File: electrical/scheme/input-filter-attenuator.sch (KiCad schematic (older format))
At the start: 13 parts, among them U4 AD8672

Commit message: a
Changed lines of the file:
@@
 $Descr A4 11693 8268
 encoding utf-8
-Sheet 2 7
+Sheet 4 7
 Title ""
 Date ""
@@
 AR Path="/55AAFE8D/55A8C542" Ref="U6"  Part="1"
 AR Path="/55AAFE9C/55A8C542" Ref="U7"  Part="1"
-F 0 "U7" H 5600 3650 60  0000 C CNN
+F 0 "U6" H 5600 3650 60  0000 C CNN
 F 1 "AD8672" H 5600 4050 60  0000 C CNN
 F 2 "Housings_SOIC:SOIC-8_3.9x4.9mm_Pitch1.27mm" H 5300 3850 60  0001 C CNN
@@
 AR Path="/55AAFE8D/55A8C549" Ref="U6"  Part="2"
 AR Path="/55AAFE9C/55A8C549" Ref="U7"  Part="2"
-F 0 "U7" H 8700 3850 60  0000 C CNN
+F 0 "U6" H 8700 3850 60  0000 C CNN
 F 1 "AD8672" H 8700 4250 60  0000 C CNN
 F 2 "Housings_SOIC:SOIC-8_3.9x4.9mm_Pitch1.27mm" H 8400 4050 60  0001 C CNN
@@
 AR Path="/55AAFE8D/55A8C74B" Ref="R57"  Part="1"
 AR Path="/55AAFE9C/55A8C74B" Ref="R63"  Part="1"
-F 0 "R63" V 5330 2800 50  0000 C CNN
+F 0 "R57" V 5330 2800 50  0000 C CNN
 F 1 "16 5%" V 5250 2800 50  0000 C CNN
 F 2 "Resistors_SMD:R_0805_HandSoldering" V 5180 2800 30  0001 C CNN
@@
 AR Path="/55AAFE8D/55A8C77D" Ref="C54"  Part="1"
 AR Path="/55AAFE9C/55A8C77D" Ref="C60"  Part="1"
-F 0 "C60" H 5025 3150 50  0000 L CNN
+F 0 "C54" H 5025 3150 50  0000 L CNN
 F 1 "100n" H 5025 2950 50  0000 L CNN
 F 2 "Capacitors_SMD:C_0805_HandSoldering" H 5038 2900 30  0001 C CNN
@@
 AR Path="/55AAFE8D/55A8C85F" Ref="#PWR0143"  Part="1"
 AR Path="/55AAFE9C/55A8C85F" Ref="#PWR0149"  Part="1"
-F 0 "#PWR0149" H 4650 2900 50  0001 C CNN
+F 0 "#PWR0143" H 4650 2900 50  0001 C CNN
 F 1 "GNDA" H 4650 3000 50  0000 C CNN
 F 2 "" H 4650 3150 60  0000 C CNN
@@
 AR Path="/55AAFE8D/55A8C8A7" Ref="R58"  Part="1"
 AR Path="/55AAFE9C/55A8C8A7" Ref="R64"  Part="1"
-F 0 "R64" V 5330 4800 50  0000 C CNN
+F 0 "R58" V 5330 4800 50  0000 C CNN
 F 1 "16 5%" V 5250 4800 50  0000 C CNN
 F 2 "Resistors_SMD:R_0805_HandSoldering" V 5180 4800 30  0001 C CNN
@@
 AR Path="/55AAFE8D/55A8CC9D" Ref="C55"  Part="1"
 AR Path="/55AAFE9C/55A8CC9D" Ref="C61"  Part="1"
-F 0 "C61" H 5025 4650 50  0000 L CNN
+F 0 "C55" H 5025 4650 50  0000 L CNN
 F 1 "100n" H 5025 4450 50  0000 L CNN
 F 2 "Capacitors_SMD:C_0805_HandSoldering" H 5038 4400 30  0001 C CNN
@@
 AR Path="/55AAFE8D/55A8CCA5" Ref="#PWR0144"  Part="1"
 AR Path="/55AAFE9C/55A8CCA5" Ref="#PWR0150"  Part="1"
-F 0 "#PWR0150" H 4650 4400 50  0001 C CNN
+F 0 "#PWR0144" H 4650 4400 50  0001 C CNN
 F 1 "GNDA" H 4650 4500 50  0000 C CNN
 F 2 "" H 4650 4650 60  0000 C CNN
@@
 AR Path="/55AAFE8D/55A8D6B2" Ref="R55"  Part="1"
 AR Path="/55AAFE9C/55A8D6B2" Ref="R61"  Part="1"
-F 0 "R61" V 3180 3650 50  0000 C CNN
+F 0 "R55" V 3180 3650 50  0000 C CNN
 F 1 "806 1%" V 3100 3650 50  0000 C CNN
 F 2 "Resistors_SMD:R_0805_HandSoldering" V 3030 3650 30  0001 C CNN
@@
 AR Path="/55AAFE8D/55A8D707" Ref="R56"  Part="1"
 AR Path="/55AAFE9C/55A8D707" Ref="R62"  Part="1"
-F 0 "R62" V 3680 3650 50  0000 C CNN
+F 0 "R56" V 3680 3650 50  0000 C CNN
 F 1 "1k91 1%" V 3600 3650 50  0000 C CNN
 F 2 "Resistors_SMD:R_0805_HandSoldering" V 3530 3650 30  0001 C CNN
@@
 AR Path="/55AAFE8D/55A8D733" Ref="C53"  Part="1"
 AR Path="/55AAFE9C/55A8D733" Ref="C59"  Part="1"
-F 0 "C59" H 3875 4000 50  0000 L CNN
+F 0 "C53" H 3875 4000 50  0000 L CNN
 F 1 "22n" H 3875 3800 50  0000 L CNN
 F 2 "Capacitors_SMD:C_0805_HandSoldering" H 3888 3750 30  0001 C CNN
@@
 AR Path="/55AAFE8D/55A8D76D" Ref="C52"  Part="1"
 AR Path="/55AAFE9C/55A8D76D" Ref="C58"  Part="1"
-F 0 "C58" H 3375 3450 50  0000 L CNN
+F 0 "C52" H 3375 3450 50  0000 L CNN
 F 1 "3u3" H 3375 3250 50  0000 L CNN
 F 2 "Capacitors_SMD:C_0805_HandSoldering" H 3388 3200 30  0001 C CNN
@@
 AR Path="/55AAFE8D/55A8D8D4" Ref="R59"  Part="1"
 AR Path="/55AAFE9C/55A8D8D4" Ref="R65"  Part="1"
-F 0 "R65" V 6280 3850 50  0000 C CNN
+F 0 "R59" V 6280 3850 50  0000 C CNN
 F 1 "9k31 1%" V 6200 3850 50  0000 C CNN
 F 2 "Resistors_SMD:R_0805_HandSoldering" V 6130 3850 30  0001 C CNN
@@
 AR Path="/55AAFE8D/55A8DA7D" Ref="R60"  Part="1"
 AR Path="/55AAFE9C/55A8DA7D" Ref="R66"  Part="1"
-F 0 "R66" V 6780 3850 50  0000 C CNN
+F 0 "R60" V 6780 3850 50  0000 C CNN
 F 1 "21k 1%" V 6700 3850 50  0000 C CNN
 F 2 "Resistors_SMD:R_0805_HandSoldering" V 6630 3850 30  0001 C CNN
@@
 AR Path="/55AAFE8D/55A8DD2D" Ref="C56"  Part="1"
 AR Path="/55AAFE9C/55A8DD2D" Ref="C62"  Part="1"
-F 0 "C62" H 6475 3700 50  0000 L CNN
+F 0 "C56" H 6475 3700 50  0000 L CNN
 F 1 "120n" H 6475 3500 50  0000 L CNN
 F 2 "Capacitors_SMD:C_0805_HandSoldering" H 6488 3450 30  0001 C CNN
@@
 AR Path="/55AAFE8D/55A8DF47" Ref="C57"  Part="1"
 AR Path="/55AAFE9C/55A8DF47" Ref="C63"  Part="1"
-F 0 "C63" H 7075 4300 50  0000 L CNN
+F 0 "C57" H 7075 4300 50  0000 L CNN
 F 1 "22n" H 7075 4100 50  0000 L CNN
 F 2 "Capacitors_SMD:C_0805_HandSoldering" H 7088 4050 30  0001 C CNN
@@
 AR Path="/55AAFE8D/55A8F5C0" Ref="#PWR0145"  Part="1"
 AR Path="/55AAFE9C/55A8F5C0" Ref="#PWR0151"  Part="1"
-F 0 "#PWR0151" H 7050 4300 50  0001 C CNN
+F 0 "#PWR0145" H 7050 4300 50  0001 C CNN
 F 1 "GNDA" H 7050 4400 50  0000 C CNN
 F 2 "" H 7050 4550 60  0000 C CNN
@@
 AR Path="/55AAFE8D/55A8F5EF" Ref="#PWR0146"  Part="1"
 AR Path="/55AAFE9C/55A8F5EF" Ref="#PWR0152"  Part="1"
-F 0 "#PWR0152" H 3850 4000 50  0001 C CNN
+F 0 "#PWR0146" H 3850 4000 50  0001 C CNN
 F 1 "GNDA" H 3850 4100 50  0000 C CNN
 F 2 "" H 3850 4250 60  0000 C CNN
@@
 AR Path="/55AAFE8D/55BB3EFD" Ref="#FLG0147"  Part="1"
 AR Path="/55AAFE9C/55BB3EFD" Ref="#FLG0153"  Part="1"
-F 0 "#FLG0153" H 5600 3045 50  0001 C CNN
+F 0 "#FLG0147" H 5600 3045 50  0001 C CNN
 F 1 "PWR_FLAG" H 5600 3130 50  0000 C CNN
 F 2 "" H 5600 2950 60  0000 C CNN
@@
 AR Path="/55A8BFF5/55BB3F68" Ref="#FLG0136"  Part="1"
 AR Path="/55AAFE9C/55BB3F68" Ref="#FLG0154"  Part="1"
-F 0 "#FLG0154" H 5600 4745 50  0001 C CNN
+F 0 "#FLG0148" H 5600 4745 50  0001 C CNN
 F 1 "PWR_FLAG" H 5600 4830 50  0000 C CNN
 F 2 "" H 5600 4650 60  0000 C CNN

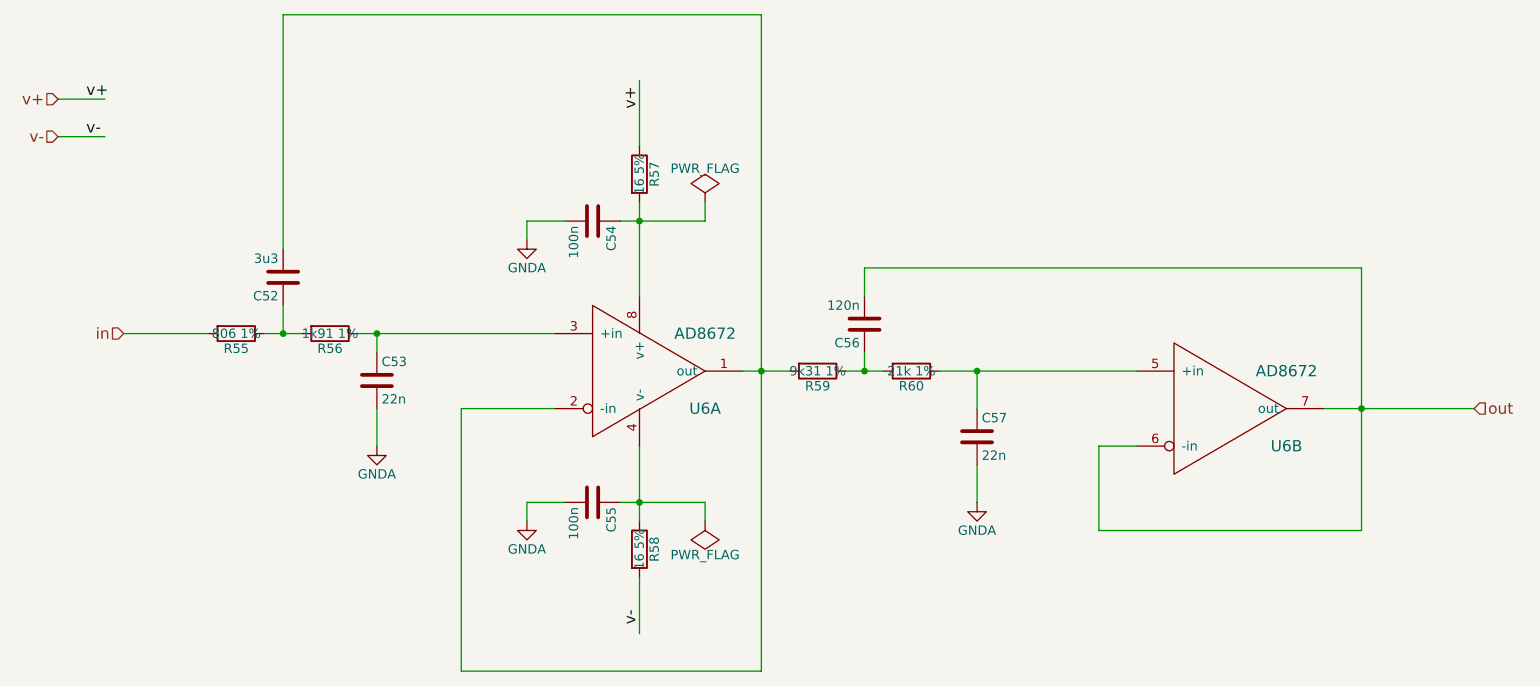
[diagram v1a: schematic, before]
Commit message: Inserted holding screw holes.
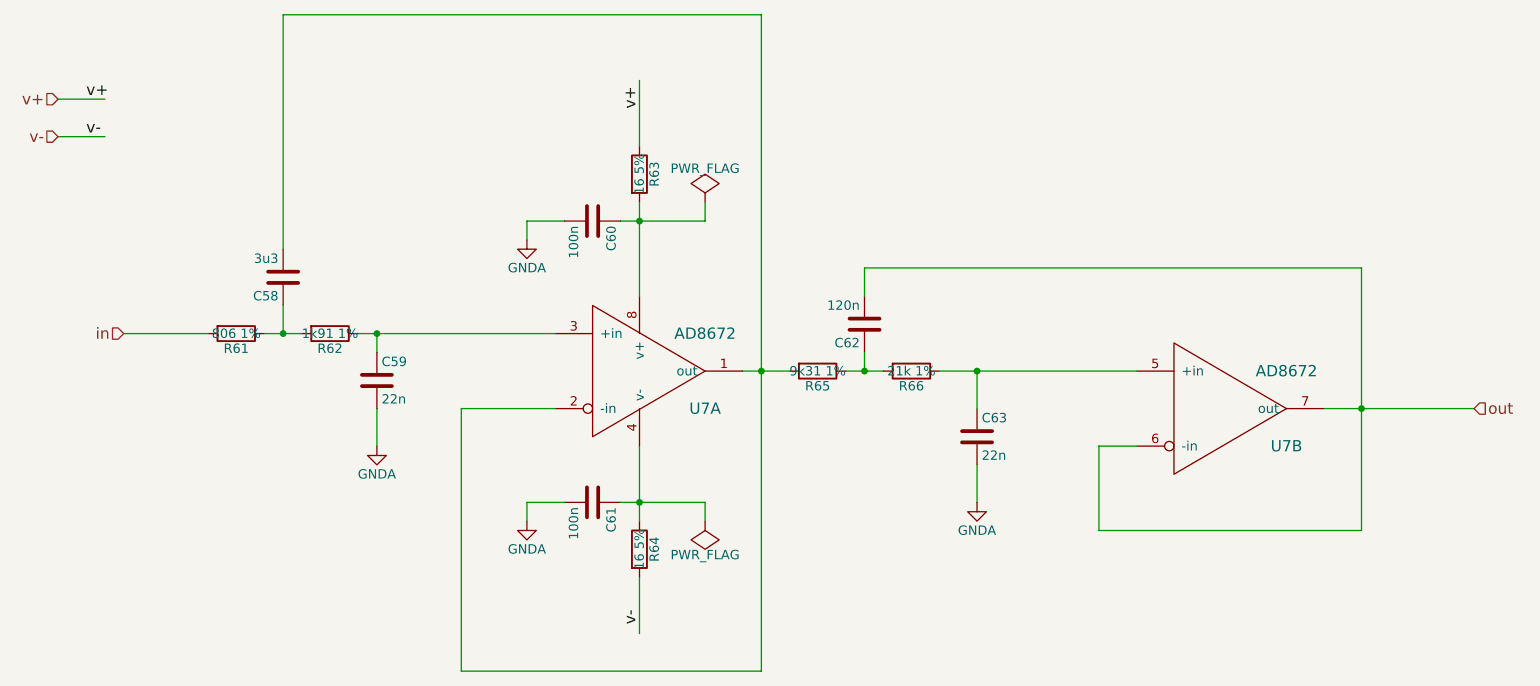
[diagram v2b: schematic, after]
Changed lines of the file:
@@
 $Descr A4 11693 8268
 encoding utf-8
-Sheet 4 7
+Sheet 5 7
 Title ""
 Date ""
@@
 AR Path="/55AAFE8D/55A8C542" Ref="U6"  Part="1"
 AR Path="/55AAFE9C/55A8C542" Ref="U7"  Part="1"
-F 0 "U6" H 5600 3650 60  0000 C CNN
+F 0 "U7" H 5600 3650 60  0000 C CNN
 F 1 "AD8672" H 5600 4050 60  0000 C CNN
 F 2 "Housings_SOIC:SOIC-8_3.9x4.9mm_Pitch1.27mm" H 5300 3850 60  0001 C CNN
@@
 AR Path="/55AAFE8D/55A8C549" Ref="U6"  Part="2"
 AR Path="/55AAFE9C/55A8C549" Ref="U7"  Part="2"
-F 0 "U6" H 8700 3850 60  0000 C CNN
+F 0 "U7" H 8700 3850 60  0000 C CNN
 F 1 "AD8672" H 8700 4250 60  0000 C CNN
 F 2 "Housings_SOIC:SOIC-8_3.9x4.9mm_Pitch1.27mm" H 8400 4050 60  0001 C CNN
@@
 AR Path="/55AAFE8D/55A8C74B" Ref="R57"  Part="1"
 AR Path="/55AAFE9C/55A8C74B" Ref="R63"  Part="1"
-F 0 "R57" V 5330 2800 50  0000 C CNN
+F 0 "R63" V 5330 2800 50  0000 C CNN
 F 1 "16 5%" V 5250 2800 50  0000 C CNN
 F 2 "Resistors_SMD:R_0805_HandSoldering" V 5180 2800 30  0001 C CNN
@@
 AR Path="/55AAFE8D/55A8C77D" Ref="C54"  Part="1"
 AR Path="/55AAFE9C/55A8C77D" Ref="C60"  Part="1"
-F 0 "C54" H 5025 3150 50  0000 L CNN
+F 0 "C60" H 5025 3150 50  0000 L CNN
 F 1 "100n" H 5025 2950 50  0000 L CNN
 F 2 "Capacitors_SMD:C_0805_HandSoldering" H 5038 2900 30  0001 C CNN
@@
 	4650 3050 4650 3150
 $Comp
-L GNDA #PWR0131
+L GNDA #PWR0135
 U 1 1 55A8C85F
 P 4650 3150
-AR Path="/55A8BFF5/55A8C85F" Ref="#PWR0131"  Part="1"
-AR Path="/55AAF91E/55A8C85F" Ref="#PWR0137"  Part="1"
-AR Path="/55AAFE8D/55A8C85F" Ref="#PWR0143"  Part="1"
-AR Path="/55AAFE9C/55A8C85F" Ref="#PWR0149"  Part="1"
-F 0 "#PWR0143" H 4650 2900 50  0001 C CNN
+AR Path="/55A8BFF5/55A8C85F" Ref="#PWR0135"  Part="1"
+AR Path="/55AAF91E/55A8C85F" Ref="#PWR0141"  Part="1"
+AR Path="/55AAFE8D/55A8C85F" Ref="#PWR0147"  Part="1"
+AR Path="/55AAFE9C/55A8C85F" Ref="#PWR0153"  Part="1"
+F 0 "#PWR0153" H 4650 2900 50  0001 C CNN
 F 1 "GNDA" H 4650 3000 50  0000 C CNN
 F 2 "" H 4650 3150 60  0000 C CNN
@@
 AR Path="/55AAFE8D/55A8C8A7" Ref="R58"  Part="1"
 AR Path="/55AAFE9C/55A8C8A7" Ref="R64"  Part="1"
-F 0 "R58" V 5330 4800 50  0000 C CNN
+F 0 "R64" V 5330 4800 50  0000 C CNN
 F 1 "16 5%" V 5250 4800 50  0000 C CNN
 F 2 "Resistors_SMD:R_0805_HandSoldering" V 5180 4800 30  0001 C CNN
@@
 AR Path="/55AAFE8D/55A8CC9D" Ref="C55"  Part="1"
 AR Path="/55AAFE9C/55A8CC9D" Ref="C61"  Part="1"
-F 0 "C55" H 5025 4650 50  0000 L CNN
+F 0 "C61" H 5025 4650 50  0000 L CNN
 F 1 "100n" H 5025 4450 50  0000 L CNN
 F 2 "Capacitors_SMD:C_0805_HandSoldering" H 5038 4400 30  0001 C CNN
@@
 	4650 4550 4650 4650
 $Comp
-L GNDA #PWR0132
+L GNDA #PWR0136
 U 1 1 55A8CCA5
 P 4650 4650
-AR Path="/55A8BFF5/55A8CCA5" Ref="#PWR0132"  Part="1"
-AR Path="/55AAF91E/55A8CCA5" Ref="#PWR0138"  Part="1"
-AR Path="/55AAFE8D/55A8CCA5" Ref="#PWR0144"  Part="1"
-AR Path="/55AAFE9C/55A8CCA5" Ref="#PWR0150"  Part="1"
-F 0 "#PWR0144" H 4650 4400 50  0001 C CNN
+AR Path="/55A8BFF5/55A8CCA5" Ref="#PWR0136"  Part="1"
+AR Path="/55AAF91E/55A8CCA5" Ref="#PWR0142"  Part="1"
+AR Path="/55AAFE8D/55A8CCA5" Ref="#PWR0148"  Part="1"
+AR Path="/55AAFE9C/55A8CCA5" Ref="#PWR0154"  Part="1"
+F 0 "#PWR0154" H 4650 4400 50  0001 C CNN
 F 1 "GNDA" H 4650 4500 50  0000 C CNN
 F 2 "" H 4650 4650 60  0000 C CNN
@@
 AR Path="/55AAFE8D/55A8D6B2" Ref="R55"  Part="1"
 AR Path="/55AAFE9C/55A8D6B2" Ref="R61"  Part="1"
-F 0 "R55" V 3180 3650 50  0000 C CNN
+F 0 "R61" V 3180 3650 50  0000 C CNN
 F 1 "806 1%" V 3100 3650 50  0000 C CNN
 F 2 "Resistors_SMD:R_0805_HandSoldering" V 3030 3650 30  0001 C CNN
@@
 AR Path="/55AAFE8D/55A8D707" Ref="R56"  Part="1"
 AR Path="/55AAFE9C/55A8D707" Ref="R62"  Part="1"
-F 0 "R56" V 3680 3650 50  0000 C CNN
+F 0 "R62" V 3680 3650 50  0000 C CNN
 F 1 "1k91 1%" V 3600 3650 50  0000 C CNN
 F 2 "Resistors_SMD:R_0805_HandSoldering" V 3530 3650 30  0001 C CNN
@@
 AR Path="/55AAFE8D/55A8D733" Ref="C53"  Part="1"
 AR Path="/55AAFE9C/55A8D733" Ref="C59"  Part="1"
-F 0 "C53" H 3875 4000 50  0000 L CNN
+F 0 "C59" H 3875 4000 50  0000 L CNN
 F 1 "22n" H 3875 3800 50  0000 L CNN
 F 2 "Capacitors_SMD:C_0805_HandSoldering" H 3888 3750 30  0001 C CNN
@@
 AR Path="/55AAFE8D/55A8D76D" Ref="C52"  Part="1"
 AR Path="/55AAFE9C/55A8D76D" Ref="C58"  Part="1"
-F 0 "C52" H 3375 3450 50  0000 L CNN
+F 0 "C58" H 3375 3450 50  0000 L CNN
 F 1 "3u3" H 3375 3250 50  0000 L CNN
 F 2 "Capacitors_SMD:C_0805_HandSoldering" H 3388 3200 30  0001 C CNN
@@
 AR Path="/55AAFE8D/55A8D8D4" Ref="R59"  Part="1"
 AR Path="/55AAFE9C/55A8D8D4" Ref="R65"  Part="1"
-F 0 "R59" V 6280 3850 50  0000 C CNN
+F 0 "R65" V 6280 3850 50  0000 C CNN
 F 1 "9k31 1%" V 6200 3850 50  0000 C CNN
 F 2 "Resistors_SMD:R_0805_HandSoldering" V 6130 3850 30  0001 C CNN
@@
 AR Path="/55AAFE8D/55A8DA7D" Ref="R60"  Part="1"
 AR Path="/55AAFE9C/55A8DA7D" Ref="R66"  Part="1"
-F 0 "R60" V 6780 3850 50  0000 C CNN
+F 0 "R66" V 6780 3850 50  0000 C CNN
 F 1 "21k 1%" V 6700 3850 50  0000 C CNN
 F 2 "Resistors_SMD:R_0805_HandSoldering" V 6630 3850 30  0001 C CNN
@@
 AR Path="/55AAFE8D/55A8DD2D" Ref="C56"  Part="1"
 AR Path="/55AAFE9C/55A8DD2D" Ref="C62"  Part="1"
-F 0 "C56" H 6475 3700 50  0000 L CNN
+F 0 "C62" H 6475 3700 50  0000 L CNN
 F 1 "120n" H 6475 3500 50  0000 L CNN
 F 2 "Capacitors_SMD:C_0805_HandSoldering" H 6488 3450 30  0001 C CNN
@@
 AR Path="/55AAFE8D/55A8DF47" Ref="C57"  Part="1"
 AR Path="/55AAFE9C/55A8DF47" Ref="C63"  Part="1"
-F 0 "C57" H 7075 4300 50  0000 L CNN
+F 0 "C63" H 7075 4300 50  0000 L CNN
 F 1 "22n" H 7075 4100 50  0000 L CNN
 F 2 "Capacitors_SMD:C_0805_HandSoldering" H 7088 4050 30  0001 C CNN
@@
 Connection ~ 9100 4050
 $Comp
-L GNDA #PWR0133
+L GNDA #PWR0137
 U 1 1 55A8F5C0
 P 7050 4550
-AR Path="/55A8BFF5/55A8F5C0" Ref="#PWR0133"  Part="1"
-AR Path="/55AAF91E/55A8F5C0" Ref="#PWR0139"  Part="1"
-AR Path="/55AAFE8D/55A8F5C0" Ref="#PWR0145"  Part="1"
-AR Path="/55AAFE9C/55A8F5C0" Ref="#PWR0151"  Part="1"
-F 0 "#PWR0145" H 7050 4300 50  0001 C CNN
+AR Path="/55A8BFF5/55A8F5C0" Ref="#PWR0137"  Part="1"
+AR Path="/55AAF91E/55A8F5C0" Ref="#PWR0143"  Part="1"
+AR Path="/55AAFE8D/55A8F5C0" Ref="#PWR0149"  Part="1"
+AR Path="/55AAFE9C/55A8F5C0" Ref="#PWR0155"  Part="1"
+F 0 "#PWR0155" H 7050 4300 50  0001 C CNN
 F 1 "GNDA" H 7050 4400 50  0000 C CNN
 F 2 "" H 7050 4550 60  0000 C CNN
@@
 $EndComp
 $Comp
-L GNDA #PWR0134
+L GNDA #PWR0138
 U 1 1 55A8F5EF
 P 3850 4250
-AR Path="/55A8BFF5/55A8F5EF" Ref="#PWR0134"  Part="1"
-AR Path="/55AAF91E/55A8F5EF" Ref="#PWR0140"  Part="1"
-AR Path="/55AAFE8D/55A8F5EF" Ref="#PWR0146"  Part="1"
-AR Path="/55AAFE9C/55A8F5EF" Ref="#PWR0152"  Part="1"
-F 0 "#PWR0146" H 3850 4000 50  0001 C CNN
+AR Path="/55A8BFF5/55A8F5EF" Ref="#PWR0138"  Part="1"
+AR Path="/55AAF91E/55A8F5EF" Ref="#PWR0144"  Part="1"
+AR Path="/55AAFE8D/55A8F5EF" Ref="#PWR0150"  Part="1"
+AR Path="/55AAFE9C/55A8F5EF" Ref="#PWR0156"  Part="1"
+F 0 "#PWR0156" H 3850 4000 50  0001 C CNN
 F 1 "GNDA" H 3850 4100 50  0000 C CNN
 F 2 "" H 3850 4250 60  0000 C CNN
@@
 	7700 4250 7900 4250
 $Comp
-L PWR_FLAG #FLG0135
+L PWR_FLAG #FLG0139
 U 1 1 55BB3EFD
 P 5600 2950
-AR Path="/55A8BFF5/55BB3EFD" Ref="#FLG0135"  Part="1"
-AR Path="/55AAF91E/55BB3EFD" Ref="#FLG0141"  Part="1"
-AR Path="/55AAFE8D/55BB3EFD" Ref="#FLG0147"  Part="1"
-AR Path="/55AAFE9C/55BB3EFD" Ref="#FLG0153"  Part="1"
-F 0 "#FLG0147" H 5600 3045 50  0001 C CNN
+AR Path="/55A8BFF5/55BB3EFD" Ref="#FLG0139"  Part="1"
+AR Path="/55AAF91E/55BB3EFD" Ref="#FLG0145"  Part="1"
+AR Path="/55AAFE8D/55BB3EFD" Ref="#FLG0151"  Part="1"
+AR Path="/55AAFE9C/55BB3EFD" Ref="#FLG0157"  Part="1"
+F 0 "#FLG0157" H 5600 3045 50  0001 C CNN
 F 1 "PWR_FLAG" H 5600 3130 50  0000 C CNN
 F 2 "" H 5600 2950 60  0000 C CNN
@@
 	5600 3050 5600 2950
 $Comp
-L PWR_FLAG #FLG0142
+L PWR_FLAG #FLG0146
 U 1 1 55BB3F68
 P 5600 4650
-AR Path="/55AAF91E/55BB3F68" Ref="#FLG0142"  Part="1"
-AR Path="/55AAFE8D/55BB3F68" Ref="#FLG0148"  Part="1"
-AR Path="/55A8BFF5/55BB3F68" Ref="#FLG0136"  Part="1"
-AR Path="/55AAFE9C/55BB3F68" Ref="#FLG0154"  Part="1"
-F 0 "#FLG0148" H 5600 4745 50  0001 C CNN
+AR Path="/55AAF91E/55BB3F68" Ref="#FLG0146"  Part="1"
+AR Path="/55AAFE8D/55BB3F68" Ref="#FLG0152"  Part="1"
+AR Path="/55A8BFF5/55BB3F68" Ref="#FLG0140"  Part="1"
+AR Path="/55AAFE9C/55BB3F68" Ref="#FLG0158"  Part="1"
+F 0 "#FLG0158" H 5600 4745 50  0001 C CNN
 F 1 "PWR_FLAG" H 5600 4830 50  0000 C CNN
 F 2 "" H 5600 4650 60  0000 C CNN

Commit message: a
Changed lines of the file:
@@
 $Descr A4 11693 8268
 encoding utf-8
-Sheet 5 7
+Sheet 3 7
 Title ""
 Date ""
@@
 AR Path="/55AAFE8D/55A8C542" Ref="U6"  Part="1"
 AR Path="/55AAFE9C/55A8C542" Ref="U7"  Part="1"
-F 0 "U7" H 5600 3650 60  0000 C CNN
+F 0 "U5" H 5600 3650 60  0000 C CNN
 F 1 "AD8672" H 5600 4050 60  0000 C CNN
 F 2 "Housings_SOIC:SOIC-8_3.9x4.9mm_Pitch1.27mm" H 5300 3850 60  0001 C CNN
@@
 AR Path="/55AAFE8D/55A8C549" Ref="U6"  Part="2"
 AR Path="/55AAFE9C/55A8C549" Ref="U7"  Part="2"
-F 0 "U7" H 8700 3850 60  0000 C CNN
+F 0 "U5" H 8700 3850 60  0000 C CNN
 F 1 "AD8672" H 8700 4250 60  0000 C CNN
 F 2 "Housings_SOIC:SOIC-8_3.9x4.9mm_Pitch1.27mm" H 8400 4050 60  0001 C CNN
@@
 AR Path="/55AAFE8D/55A8C74B" Ref="R57"  Part="1"
 AR Path="/55AAFE9C/55A8C74B" Ref="R63"  Part="1"
-F 0 "R63" V 5330 2800 50  0000 C CNN
+F 0 "R51" V 5330 2800 50  0000 C CNN
 F 1 "16 5%" V 5250 2800 50  0000 C CNN
 F 2 "Resistors_SMD:R_0805_HandSoldering" V 5180 2800 30  0001 C CNN
@@
 AR Path="/55AAFE8D/55A8C77D" Ref="C54"  Part="1"
 AR Path="/55AAFE9C/55A8C77D" Ref="C60"  Part="1"
-F 0 "C60" H 5025 3150 50  0000 L CNN
+F 0 "C48" H 5025 3150 50  0000 L CNN
 F 1 "100n" H 5025 2950 50  0000 L CNN
 F 2 "Capacitors_SMD:C_0805_HandSoldering" H 5038 2900 30  0001 C CNN
@@
 AR Path="/55AAFE8D/55A8C8A7" Ref="R58"  Part="1"
 AR Path="/55AAFE9C/55A8C8A7" Ref="R64"  Part="1"
-F 0 "R64" V 5330 4800 50  0000 C CNN
+F 0 "R52" V 5330 4800 50  0000 C CNN
 F 1 "16 5%" V 5250 4800 50  0000 C CNN
 F 2 "Resistors_SMD:R_0805_HandSoldering" V 5180 4800 30  0001 C CNN
@@
 AR Path="/55AAFE8D/55A8CC9D" Ref="C55"  Part="1"
 AR Path="/55AAFE9C/55A8CC9D" Ref="C61"  Part="1"
-F 0 "C61" H 5025 4650 50  0000 L CNN
+F 0 "C49" H 5025 4650 50  0000 L CNN
 F 1 "100n" H 5025 4450 50  0000 L CNN
 F 2 "Capacitors_SMD:C_0805_HandSoldering" H 5038 4400 30  0001 C CNN
@@
 AR Path="/55AAFE8D/55A8D6B2" Ref="R55"  Part="1"
 AR Path="/55AAFE9C/55A8D6B2" Ref="R61"  Part="1"
-F 0 "R61" V 3180 3650 50  0000 C CNN
+F 0 "R49" V 3180 3650 50  0000 C CNN
 F 1 "806 1%" V 3100 3650 50  0000 C CNN
 F 2 "Resistors_SMD:R_0805_HandSoldering" V 3030 3650 30  0001 C CNN
@@
 AR Path="/55AAFE8D/55A8D707" Ref="R56"  Part="1"
 AR Path="/55AAFE9C/55A8D707" Ref="R62"  Part="1"
-F 0 "R62" V 3680 3650 50  0000 C CNN
+F 0 "R50" V 3680 3650 50  0000 C CNN
 F 1 "1k91 1%" V 3600 3650 50  0000 C CNN
 F 2 "Resistors_SMD:R_0805_HandSoldering" V 3530 3650 30  0001 C CNN
@@
 AR Path="/55AAFE8D/55A8D733" Ref="C53"  Part="1"
 AR Path="/55AAFE9C/55A8D733" Ref="C59"  Part="1"
-F 0 "C59" H 3875 4000 50  0000 L CNN
+F 0 "C47" H 3875 4000 50  0000 L CNN
 F 1 "22n" H 3875 3800 50  0000 L CNN
 F 2 "Capacitors_SMD:C_0805_HandSoldering" H 3888 3750 30  0001 C CNN
@@
 AR Path="/55AAFE8D/55A8D76D" Ref="C52"  Part="1"
 AR Path="/55AAFE9C/55A8D76D" Ref="C58"  Part="1"
-F 0 "C58" H 3375 3450 50  0000 L CNN
+F 0 "C46" H 3375 3450 50  0000 L CNN
 F 1 "3u3" H 3375 3250 50  0000 L CNN
 F 2 "Capacitors_SMD:C_0805_HandSoldering" H 3388 3200 30  0001 C CNN
@@
 AR Path="/55AAFE8D/55A8D8D4" Ref="R59"  Part="1"
 AR Path="/55AAFE9C/55A8D8D4" Ref="R65"  Part="1"
-F 0 "R65" V 6280 3850 50  0000 C CNN
+F 0 "R53" V 6280 3850 50  0000 C CNN
 F 1 "9k31 1%" V 6200 3850 50  0000 C CNN
 F 2 "Resistors_SMD:R_0805_HandSoldering" V 6130 3850 30  0001 C CNN
@@
 AR Path="/55AAFE8D/55A8DA7D" Ref="R60"  Part="1"
 AR Path="/55AAFE9C/55A8DA7D" Ref="R66"  Part="1"
-F 0 "R66" V 6780 3850 50  0000 C CNN
+F 0 "R54" V 6780 3850 50  0000 C CNN
 F 1 "21k 1%" V 6700 3850 50  0000 C CNN
 F 2 "Resistors_SMD:R_0805_HandSoldering" V 6630 3850 30  0001 C CNN
@@
 AR Path="/55AAFE8D/55A8DD2D" Ref="C56"  Part="1"
 AR Path="/55AAFE9C/55A8DD2D" Ref="C62"  Part="1"
-F 0 "C62" H 6475 3700 50  0000 L CNN
+F 0 "C50" H 6475 3700 50  0000 L CNN
 F 1 "120n" H 6475 3500 50  0000 L CNN
 F 2 "Capacitors_SMD:C_0805_HandSoldering" H 6488 3450 30  0001 C CNN
@@
 AR Path="/55AAFE8D/55A8DF47" Ref="C57"  Part="1"
 AR Path="/55AAFE9C/55A8DF47" Ref="C63"  Part="1"
-F 0 "C63" H 7075 4300 50  0000 L CNN
+F 0 "C51" H 7075 4300 50  0000 L CNN
 F 1 "22n" H 7075 4100 50  0000 L CNN
 F 2 "Capacitors_SMD:C_0805_HandSoldering" H 7088 4050 30  0001 C CNN
